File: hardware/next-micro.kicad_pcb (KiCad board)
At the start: 2 copper layers, 17.8 x 33 mm, 26 parts, among them J1 USB_C_Receptacle_USB2.0, J2 Conn_01x13, J3 Conn_01x05, J4 Conn_01x13, SW1 RESET, U1 ATmega32U4-M, U2 RT9013-33GB, Y1 8MHz

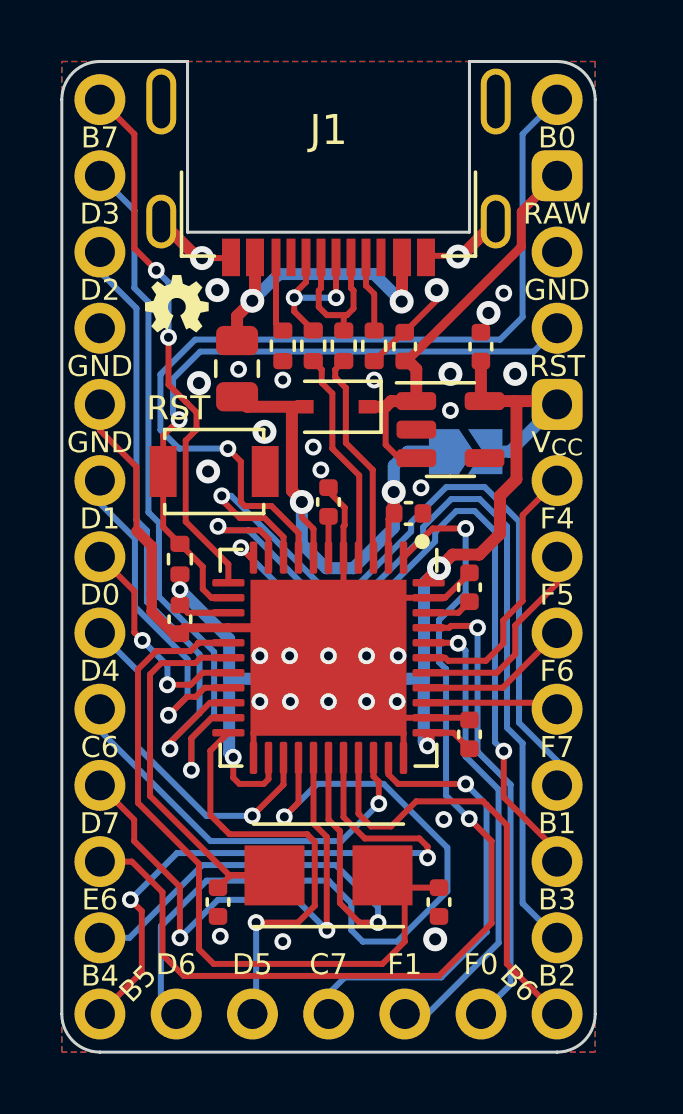
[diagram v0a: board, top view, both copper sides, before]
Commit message: Replace D1 footprint to hand soldering version
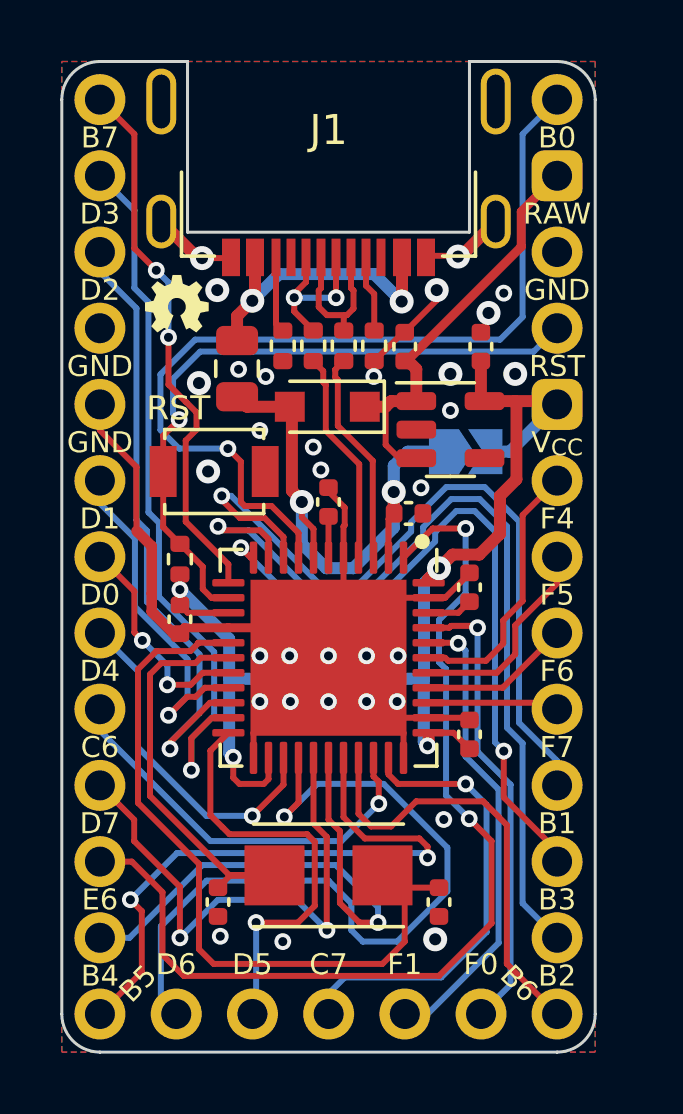
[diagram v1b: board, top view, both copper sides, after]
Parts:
- D1: footprint Diode_SMD:D_SOD-323 -> Diode_SMD:D_SOD-323_HandSoldering
- moved D1 0.29 mm to (191.7, 124.5)
